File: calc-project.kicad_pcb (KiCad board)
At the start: 2 copper layers, 39 parts, among them J1 PinSocket_1x20_Right, J2 PinSocket_1x20_Left, J3 Conn_01x14, SW1 SW_Push_45deg, SW10 SW_Push_45deg, SW11 SW_Push_45deg, SW12 SW_Push_45deg, SW13 SW_Push_45deg, SW14 SW_Push_45deg, SW15 SW_Push_45deg, SW16 SW_Push_45deg, SW17 SW_Push_45deg, SW18 SW_Push_45deg, SW19 SW_Push_45deg, SW2 SW_Push_45deg, SW20 SW_Push_45deg, SW21 SW_Push_45deg, SW22 SW_Push_45deg, SW23 SW_Push_45deg, SW24 SW_Push_45deg, SW25 SW_Push_45deg, SW26 SW_Push_45deg, SW27 SW_Push_45deg, SW28 SW_Push_45deg, SW29 SW_Push_45deg, SW3 SW_Push_45deg, SW30 SW_Push_45deg, SW31 SW_Push_45deg, SW32 SW_Push_45deg, SW33 SW_Push_45deg, SW34 SW_Push_45deg, SW35 SW_Push_45deg, SW36 SW_Push_45deg, SW4 SW_Push_45deg, SW5 SW_Push_45deg, SW6 SW_Push_45deg, SW7 SW_Push_45deg, SW8 SW_Push_45deg, SW9 SW_Push_45deg

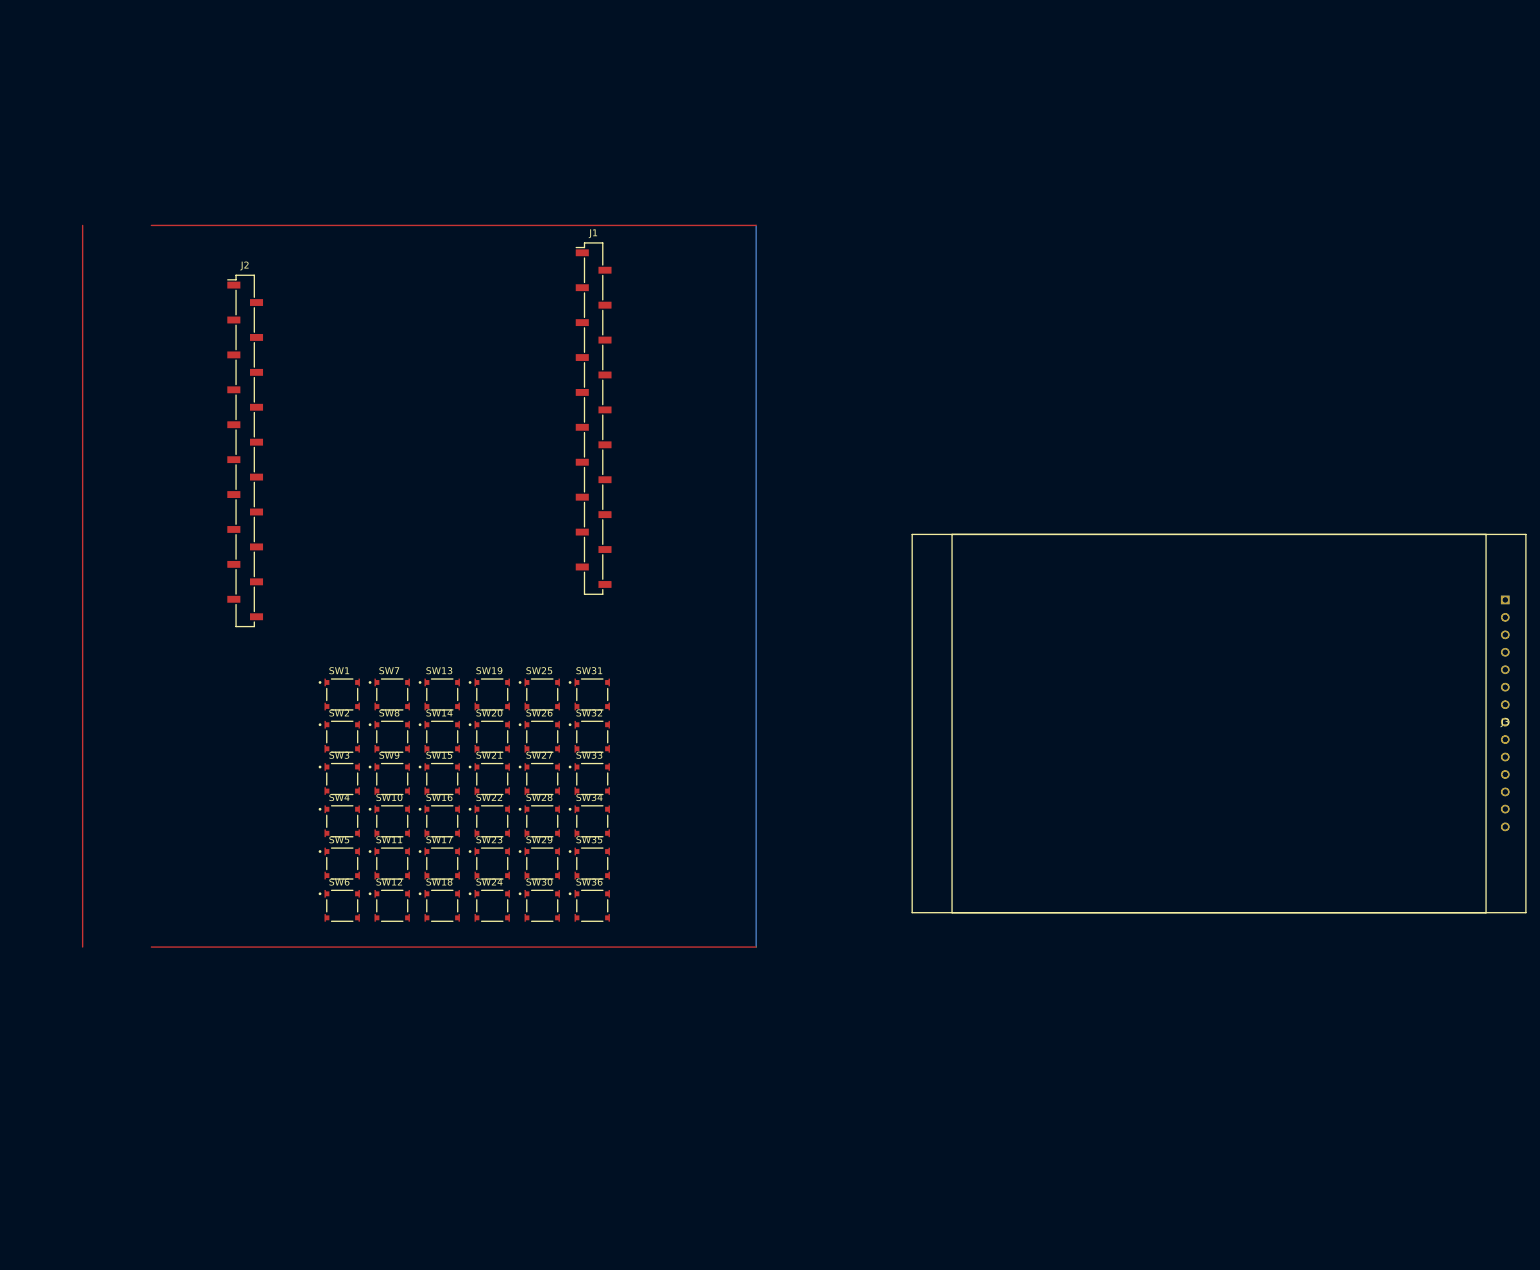
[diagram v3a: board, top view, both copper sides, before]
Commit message: edited some stuff
fixed footprint, wired up, moved screen
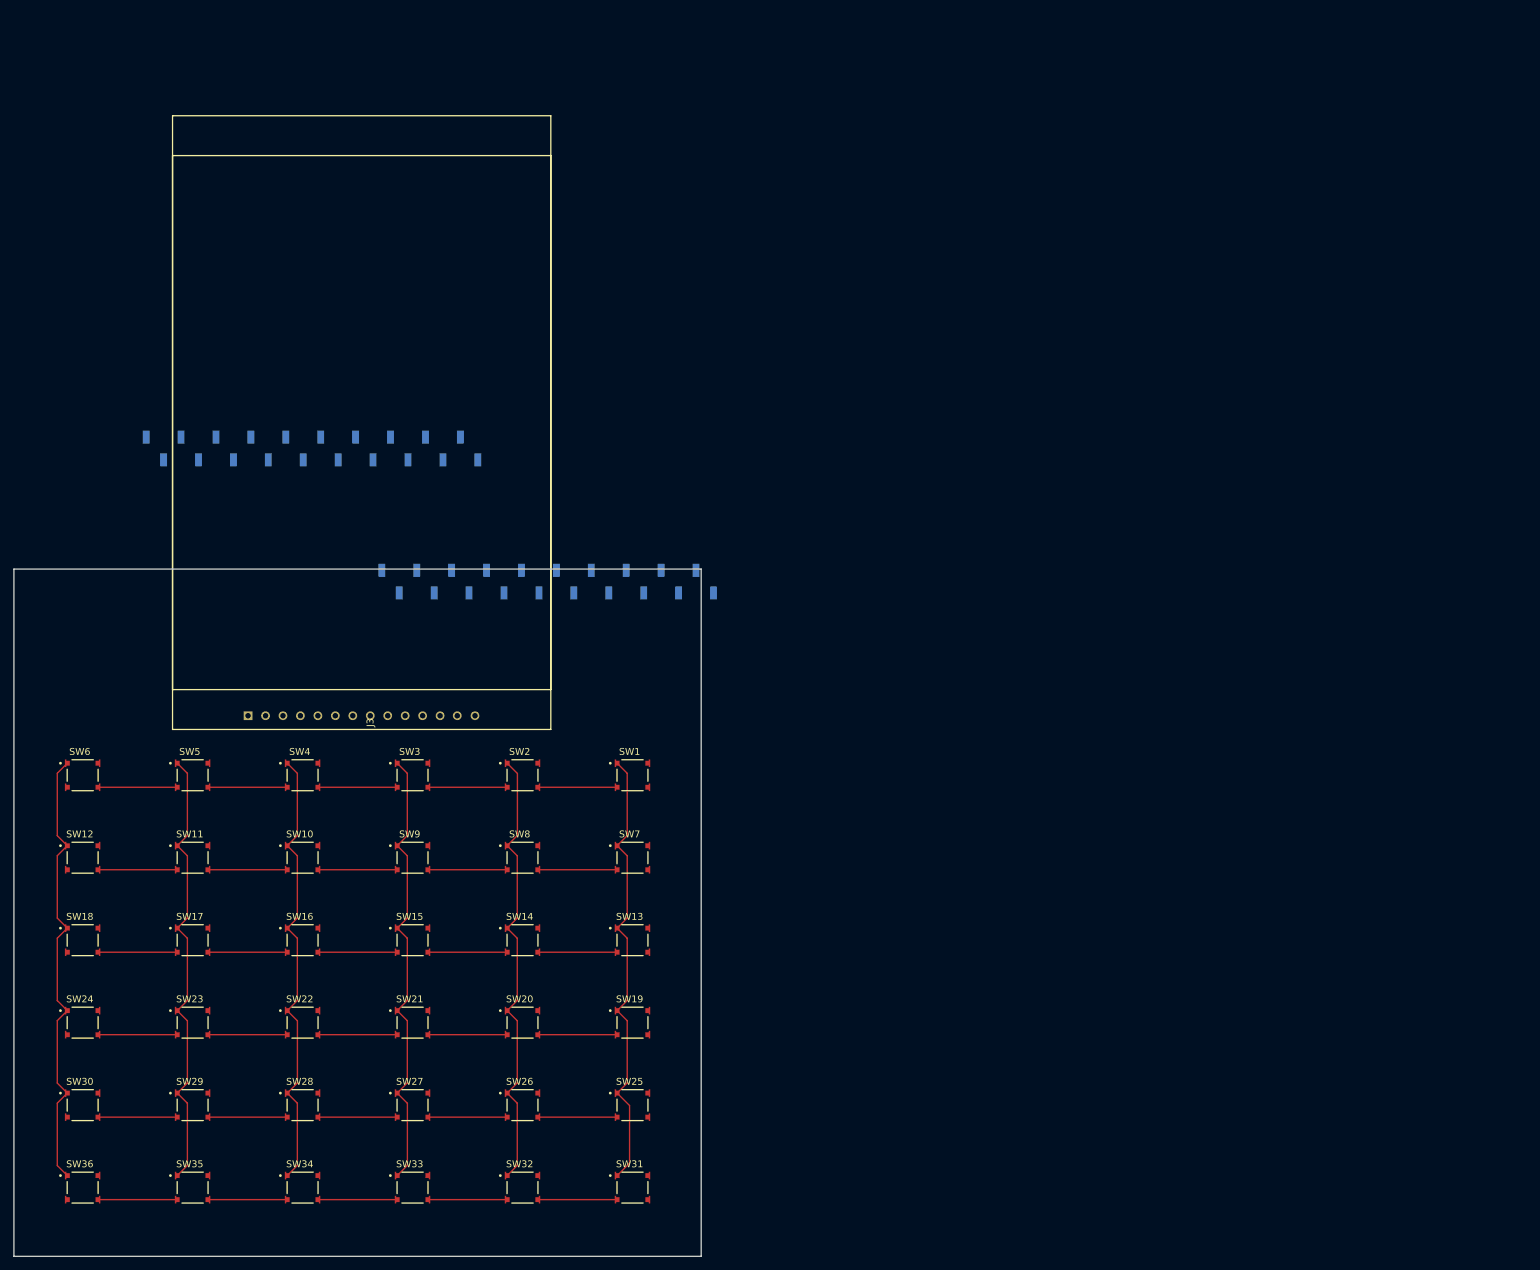
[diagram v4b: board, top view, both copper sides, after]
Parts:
- J1, J2: moved to B.Cu
- moved J3 166.4 mm to (80.6, 111.3), turned to 90 degrees
- moved SW36 84.7 mm to (40.0, 180.0)
- moved SW35 74.9 mm to (56.0, 180.0)
- moved SW30 72.9 mm to (40.0, 168.0)
- moved SW31 72.0 mm to (120.0, 180.0)
- moved SW34 68.0 mm to (72.0, 180.0)
- moved SW32 66.4 mm to (104.0, 180.0)
- moved SW33 64.9 mm to (88.0, 180.0)
- moved SW24 62.0 mm to (40.0, 156.0)
- moved SW29 61.8 mm to (56.0, 168.0)
- moved SW25 61.2 mm to (120.0, 168.0)
- moved SW28 54.1 mm to (72.0, 168.0)
- moved SW26 53.7 mm to (104.0, 168.0)
- moved SW18 52.6 mm to (40.0, 144.0)
- moved SW19 51.9 mm to (120.0, 156.0)
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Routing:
- net col 5: track 0.00 -> 66.4 mm
- net col 4: track 0.00 -> 66.1 mm
- net col 3: track 0.00 -> 66.1 mm
- net col 2: track 0.00 -> 66.1 mm
- net col 1: track 0.00 -> 66.1 mm
- net col 0: track 0.00 -> 66.0 mm
- net row 5: track 0.00 -> 57.7 mm
- net row 4: track 0.00 -> 57.7 mm
- net row 3: track 0.00 -> 57.7 mm
- net row 2: track 0.00 -> 57.7 mm
- net row 1: track 0.00 -> 57.7 mm
- net row 0: track 0.00 -> 57.7 mm
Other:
- board outline added: 100 x 100 mm

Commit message: idk
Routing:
- net col 5: track 66.4 -> 91.0 mm
- net col 2: track 66.1 -> 69.3 mm
- net col 4: track 66.1 -> 69.3 mm
- net col 3: track 66.1 -> 69.0 mm
- net col 1: track 66.1 -> 68.9 mm

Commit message: routing
routing
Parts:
- SW1, SW10, SW11, SW12, SW13, SW14, SW15, SW16, SW17, SW18, SW19, SW2, SW20, SW21, SW22, SW23, SW24, SW25, SW26, SW27, SW28, SW29, SW3, SW30, SW31, SW32, SW33, SW34, SW35, SW36, SW4, SW5, SW6, SW7, SW8, SW9: footprint Library:SW_TL3315NF160Q -> Library:SW_PUSH_6mm_centered
- moved SW1 80.6 mm to (40.0, 110.0)
- moved SW6 80.6 mm to (120.0, 110.0)
- moved SW12 80.0 mm to (120.0, 132.0)
- moved SW13 80.0 mm to (40.0, 144.0)
- moved SW18 80.0 mm to (120.0, 144.0)
- moved SW19 80.0 mm to (40.0, 156.0)
- moved SW24 80.0 mm to (120.0, 156.0)
- moved SW25 80.0 mm to (40.0, 168.0)
- moved SW30 80.0 mm to (120.0, 168.0)
- moved SW31 80.0 mm to (40.0, 180.0)
- moved SW36 80.0 mm to (120.0, 180.0)
- moved SW7 80.0 mm to (40.0, 132.0)
- moved SW2 49.0 mm to (56.0, 110.0)
- moved SW5 49.0 mm to (104.0, 110.0)
- moved SW11 48.0 mm to (104.0, 132.0)
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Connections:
- J1 pad 28: GND -> unconnected-(J1-GND-Pad28)
- J1 pad 38: GND -> unconnected-(J1-GND-Pad38)
- J1 pad 39: VSYS(3-5V) -> unconnected-(J1-VSYS-Pad39)
- J2 pad 18: GND -> unconnected-(J2-GND-Pad18)
- J2 pad 3: GND -> unconnected-(J2-GND-Pad3)
- J2 pad 8: GND -> unconnected-(J2-GND-Pad8)
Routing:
- net col 4: track 69.3 -> 166.2 mm, vias 0 -> 2
- net row 5: track 57.7 -> 152.1 mm, vias 0 -> 1
- net col 5: track 91.0 -> 179.8 mm, vias 0 -> 2
- net col 3: track 69.0 -> 153.6 mm, vias 0 -> 2
- net col 2: track 69.3 -> 140.5 mm, vias 0 -> 1
- net col 1: track 68.9 -> 127.3 mm
- net +3.3V: track 0.00 -> 57.4 mm
- net col 0: track 66.0 -> 116.0 mm
- net row 4: track 57.7 -> 98.6 mm, vias 0 -> 1
- net row 3: track 57.7 -> 90.7 mm
- net RESET: track 0.00 -> 27.7 mm, vias 0 -> 1
- net GND: track 0.00 -> 20.8 mm
- net row 2: track 57.7 -> 77.2 mm
- net LED_CTRL: track 0.00 -> 19.0 mm
- net CS: track 0.00 -> 15.3 mm
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
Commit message: capabilities
yeah
did use kicad happy just to check and make sure we had capabilities
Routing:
- net row 0: track 58.6 -> 99.6 mm
- net row 3: track 90.7 -> 131.3 mm
- net row 4: track 98.6 -> 137.6 mm
- net row 2: track 77.2 -> 116.2 mm
- net row 1: track 64.5 -> 103.5 mm
- net col 5: track 179.8 -> 188.3 mm
- net col 4: track 166.2 -> 174.4 mm
- net col 1: track 127.3 -> 133.8 mm
- net col 3: track 153.6 -> 160.0 mm
- net col 2: track 140.5 -> 146.8 mm
- net RESET: track 27.7 -> 25.5 mm
- net +3.3V: track 57.4 -> 58.1 mm

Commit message: wrong pin
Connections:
- J2 pad 13: row 4 -> unconnected-(J2-GND-Pad13)
- J2 pad 14: row 5 -> row 4
- J2 pad 15: unconnected-(J2-GP11-Pad15) -> row 5
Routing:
- net row 4: track 137.6 -> 141.9 mm
- net RESET: track 25.5 -> 22.9 mm
- net row 0: track 99.6 -> 98.4 mm
- net row 5: track 152.1 -> 151.0 mm
